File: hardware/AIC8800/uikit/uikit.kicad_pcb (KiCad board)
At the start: 2 copper layers, 36 parts, among them J1 Conn_01x20, J2 Conn_01x20, J3 Conn_01x10, J4 Conn_01x06, J5 USB_C_Receptacle_USB2.0, J6 Micro_SD_Card, J7 PJ-393-USA, U1 AIC1000A, U2 CH340N

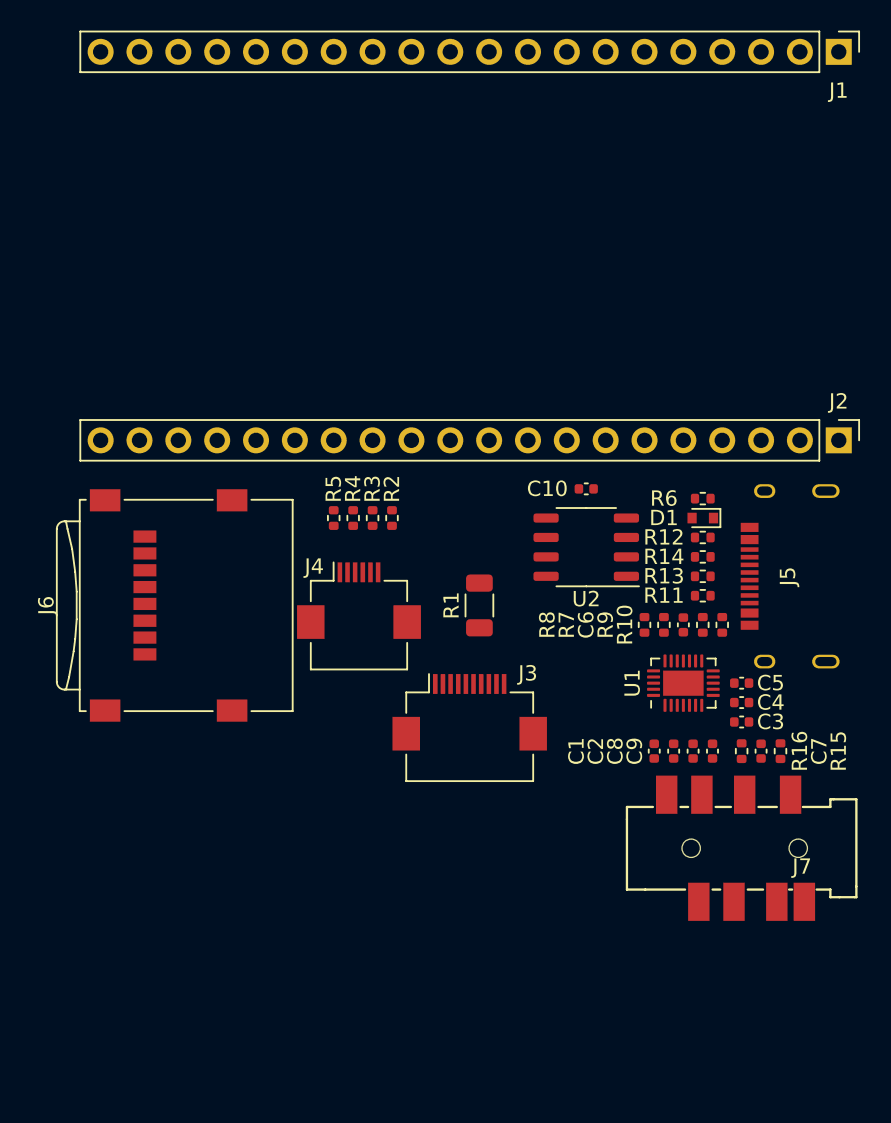
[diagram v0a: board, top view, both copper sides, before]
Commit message: [hardware/AIC8800/uikit] update PCB
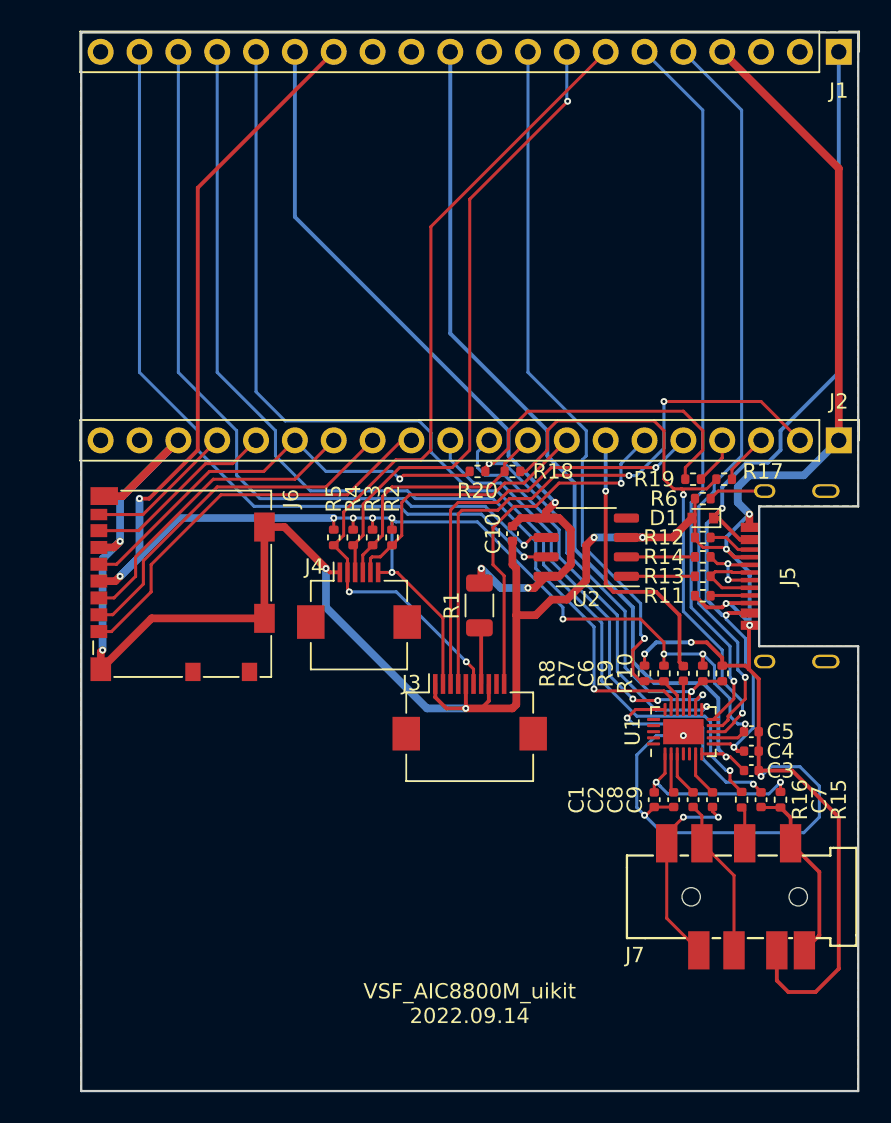
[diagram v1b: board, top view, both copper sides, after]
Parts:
- added R17: 0, Resistor_SMD:R_0402_1005Metric, F.Cu at (245.2, 118.1)
- added R18: NC, Resistor_SMD:R_0402_1005Metric, F.Cu at (231.4, 117.6)
- added R19: 0, Resistor_SMD:R_0402_1005Metric, F.Cu at (243.2, 118.1)
- added R20: NC, Resistor_SMD:R_0402_1005Metric, F.Cu at (229.1, 117.6)
- J6: value Micro_SD_Card -> Micro_SD_Card_Det; footprint Connector_Card:microSD_HC_Wuerth_693072010801 -> Connector_Card:microSD_HC_Molex_104031-0811
- moved C10 5.64 mm to (231.4, 121.7), turned to -90 degrees
- moved C5 3.24 mm to (247.0, 134.6)
- moved C3 3.24 mm to (247.0, 137.2), turned to 180 degrees
- moved C4 3.24 mm to (247.0, 135.9)
- moved C1 3.18 mm to (240.7, 139.1)
- moved C2 3.18 mm to (241.9, 139.1)
- moved C7 3.18 mm to (247.7, 139.1)
- moved C8 3.18 mm to (243.2, 139.1)
- moved C9 3.18 mm to (244.5, 139.1)
- moved R15 3.18 mm to (248.9, 139.1)
- moved R16 3.18 mm to (246.4, 139.1)
- moved U1 3.18 mm to (242.6, 134.6)
- moved C6 3.17 mm to (242.6, 130.8)
- moved R10 3.17 mm to (245.1, 130.8)
- moved R7 3.17 mm to (241.3, 130.8)
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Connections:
- R10 pad 2: /A2 -> /I2S_DIN
- R9 pad 2: /A2 -> /I2S_DIN
- U1 pad 10: /A1 -> /I2S_BCK
- U1 pad 15: /A2 -> /I2S_DIN
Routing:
- net GND: track 0.00 -> 234.5 mm, vias 0 -> 15
- net /VCC: track 0.00 -> 112.9 mm, vias 0 -> 11
- net /B4: track 0.00 -> 70.5 mm, vias 0 -> 1
- net /AU_PWR: track 0.00 -> 64.6 mm, vias 0 -> 1
- net /USB_5V: track 0.00 -> 59.4 mm, vias 0 -> 3
- net /V13: track 0.00 -> 58.7 mm, vias 0 -> 1
- net /B1: track 0.00 -> 55.3 mm, vias 0 -> 2
- net /B7: track 0.00 -> 53.3 mm, vias 0 -> 1
- net /V33: track 0.00 -> 52.4 mm, vias 0 -> 3
- net /B6: track 0.00 -> 51.6 mm, vias 0 -> 1
- net /AU_SDA: track 0.00 -> 49.3 mm, vias 0 -> 1
- net /AU_SLEEP: track 0.00 -> 48.8 mm, vias 0 -> 1
- net /AU_SCL: track 0.00 -> 47.3 mm, vias 0 -> 1
- net /I2S_DIN: track 0.00 -> 47.0 mm, vias 0 -> 2
- net /B2: track 0.00 -> 41.9 mm, vias 0 -> 1
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- added copper zone on B.Cu, net GND
- added copper zone on F.Cu, net GND
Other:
- board outline added: 50.8 x 69.2 mm
- board text added: "VSF_AIC8800M_uikit 2022.09.14"

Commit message: [hardware/AIC8800/uikit] update PCB
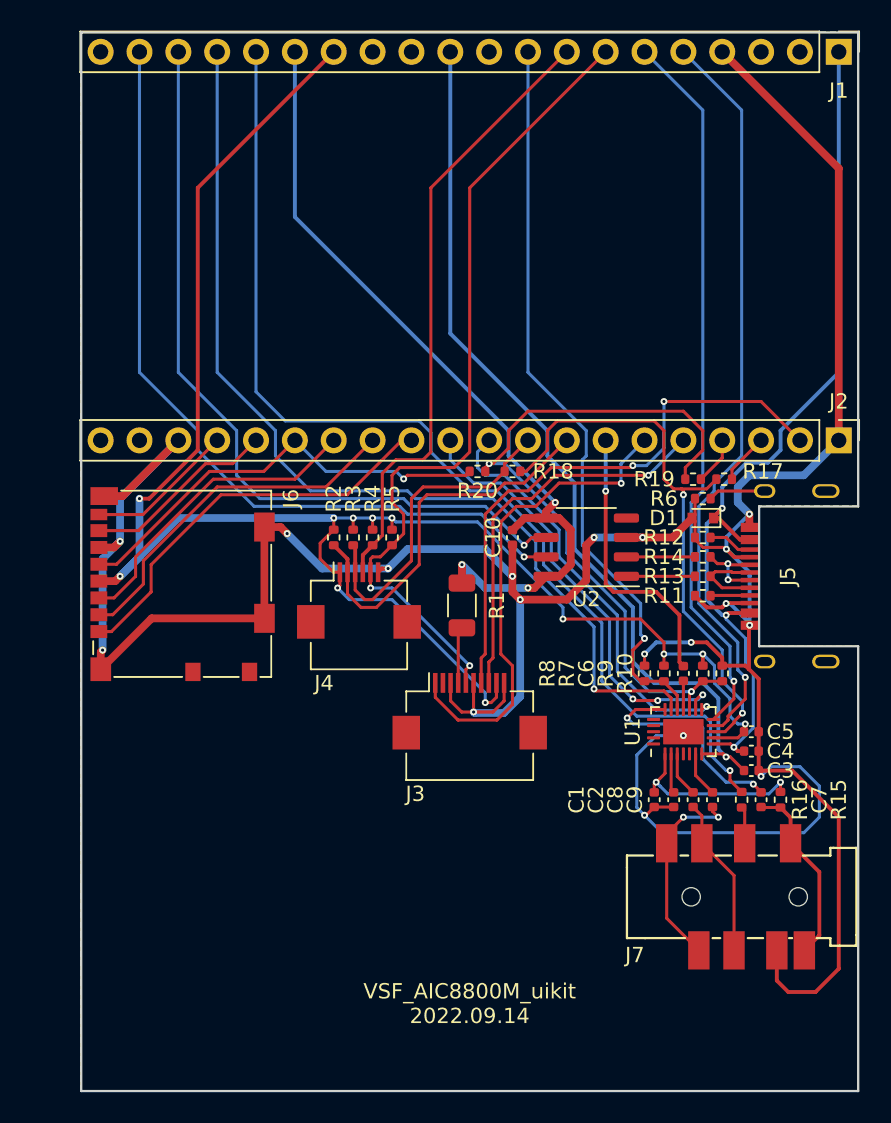
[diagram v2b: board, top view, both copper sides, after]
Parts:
- J3: footprint Connector_FFC-FPC:Hirose_FH12-10S-0.5SH_1x10-1MP_P0.50mm_Horizontal -> VSF:Hirose_FH12-10S-0.5SH_1x10-1MP_P0.50mm_Horizontal_Reverse
- J4: footprint Connector_FFC-FPC:Hirose_FH12-6S-0.5SH_1x06-1MP_P0.50mm_Horizontal -> VSF:Hirose_FH12-6S-0.5SH_1x06-1MP_P0.50mm_Horizontal_Reverse
- moved R2 3.81 mm to (219.7, 121.9)
- moved R5 3.81 mm to (223.5, 121.9)
- moved R3 1.27 mm to (221.0, 121.9)
- moved R4 1.27 mm to (222.2, 121.9)
- moved R1 1.14 mm to (228.1, 126.4)
- moved C10 0.25 mm to (231.4, 121.9)
- moved J4 0.06 mm to (221.4, 126.1)
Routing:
- net /A4: track 23.6 -> 31.7 mm
- net /A6: track 18.2 -> 25.2 mm
- net /VCC: track 112.9 -> 119.5 mm, vias 11 -> 12
- net /A7: track 16.8 -> 21.5 mm
- net /A3: track 28.5 -> 25.4 mm
- net /A0: track 39.4 -> 37.6 mm
- net /V33: track 52.4 -> 54.1 mm
- net GND: track 234.5 -> 232.8 mm, vias 15 -> 18
- net /B2: track 41.9 -> 40.6 mm, vias 1 -> 0
- net /B1: track 55.3 -> 54.3 mm

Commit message: [hardware/AIC8800/uikit] minor tweak
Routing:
- net /B2: track 40.6 -> 41.1 mm
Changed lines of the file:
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@@
   (segment (start 243.84 129.54) (end 243.84 130.3) (width 0.254) (layer "F.Cu") (net 8))
   (segment (start 230.35 131.43) (end 230.35 132.362) (width 0.2) (layer "F.Cu") (net 8))
-  (segment (start 218.821 123.317) (end 218.821 122.299) (width 0.2) (layer "F.Cu") (net 8))
+  (segment (start 218.948 122.172) (end 219.71 121.41) (width 0.2) (layer "F.Cu") (net 8))
   (segment (start 220.111 124.191) (end 220.111 125.075) (width 0.2) (layer "F.Cu") (net 8))
   (segment (start 205.427 124.773) (end 205.74 124.46) (width 0.508) (layer "F.Cu") (net 8))
-  (segment (start 218.821 122.299) (end 219.71 121.41) (width 0.2) (layer "F.Cu") (net 8))
   (segment (start 229.997 132.715) (end 229.616 132.715) (width 0.2) (layer "F.Cu") (net 8))
   (segment (start 223.52 121.41) (end 223.52 120.65) (width 0.2) (layer "F.Cu") (net 8))
   (segment (start 244.52 135.02) (end 246.135 135.02) (width 0.2) (layer "F.Cu") (net 8))
+  (segment (start 218.948 122.936) (end 218.948 122.172) (width 0.2) (layer "F.Cu") (net 8))
   (segment (start 241.3 128.778) (end 241.3 129.54) (width 0.2) (layer "F.Cu") (net 8))
   (segment (start 246.535 134.62) (end 246.535 134.194479) (width 0.2) (layer "F.Cu") (net 8))
@@
   (segment (start 230.35 132.362) (end 229.997 132.715) (width 0.2) (layer "F.Cu") (net 8))
   (segment (start 220.111 125.075) (end 219.964 125.222) (width 0.2) (layer "F.Cu") (net 8))
-  (segment (start 220.111 124.191) (end 219.695 124.191) (width 0.2) (layer "F.Cu") (net 8))
   (segment (start 241.3 130.3) (end 241.3 129.54) (width 0.2) (layer "F.Cu") (net 8))
+  (segment (start 220.111 124.191) (end 220.111 124.099) (width 0.2) (layer "F.Cu") (net 8))
   (segment (start 239.776 127.254) (end 241.3 128.778) (width 0.2) (layer "F.Cu") (net 8))
   (segment (start 210.82 116.205) (end 207.645 119.38) (width 0.254) (layer "F.Cu") (net 8))
   (segment (start 246.135 135.02) (end 246.535 134.62) (width 0.2) (layer "F.Cu") (net 8))
-  (segment (start 219.695 124.191) (end 218.821 123.317) (width 0.2) (layer "F.Cu") (net 8))
+  (segment (start 220.111 124.099) (end 218.948 122.936) (width 0.2) (layer "F.Cu") (net 8))
   (via (at 219.964 125.222) (size 0.45212) (drill 0.2032) (layers "F.Cu" "B.Cu") (net 8))
   (via (at 241.3 129.54) (size 0.45212) (drill 0.2032) (layers "F.Cu" "B.Cu") (net 8))
@@
   (segment (start 222.111 123.329) (end 222.25 123.19) (width 0.2) (layer "F.Cu") (net 22))
   (segment (start 228.35 131.43) (end 228.35 130.552) (width 0.2) (layer "F.Cu") (net 22))
-  (segment (start 224.028 117.348) (end 223.52 117.856) (width 0.2) (layer "F.Cu") (net 22))
-  (segment (start 224.282 121.668) (end 223.52 122.43) (width 0.2) (layer "F.Cu") (net 22))
+  (segment (start 223.52 122.43) (end 222.885 121.795) (width 0.2) (layer "F.Cu") (net 22))
   (segment (start 222.123 125.222) (end 222.111 125.21) (width 0.2) (layer "F.Cu") (net 22))
   (segment (start 228.6 116.332) (end 227.584 117.348) (width 0.2) (layer "F.Cu") (net 22))
   (segment (start 227.584 117.348) (end 224.028 117.348) (width 0.2) (layer "F.Cu") (net 22))
-  (segment (start 223.52 119.634) (end 224.282 120.396) (width 0.2) (layer "F.Cu") (net 22))
   (segment (start 228.35 130.552) (end 228.6 130.302) (width 0.2) (layer "F.Cu") (net 22))
   (segment (start 223.518 122.43) (end 223.52 122.43) (width 0.2) (layer "F.Cu") (net 22))
   (segment (start 222.111 124.191) (end 222.111 123.329) (width 0.2) (layer "F.Cu") (net 22))
+  (segment (start 222.885 118.491) (end 224.028 117.348) (width 0.2) (layer "F.Cu") (net 22))
   (segment (start 222.25 123.19) (end 222.758 123.19) (width 0.2) (layer "F.Cu") (net 22))
+  (segment (start 222.885 121.795) (end 222.885 118.491) (width 0.2) (layer "F.Cu") (net 22))
   (segment (start 222.758 123.19) (end 223.518 122.43) (width 0.2) (layer "F.Cu") (net 22))
-  (segment (start 223.52 117.856) (end 223.52 119.634) (width 0.2) (layer "F.Cu") (net 22))
   (segment (start 228.6 99.06) (end 228.6 116.332) (width 0.2) (layer "F.Cu") (net 22))
   (segment (start 222.111 125.21) (end 222.111 124.191) (width 0.2) (layer "F.Cu") (net 22))
-  (segment (start 224.282 120.396) (end 224.282 121.668) (width 0.2) (layer "F.Cu") (net 22))
   (segment (start 237.49 90.17) (end 228.6 99.06) (width 0.2) (layer "F.Cu") (net 22))
   (via (at 222.123 125.222) (size 0.45212) (drill 0.2032) (layers "F.Cu" "B.Cu") (net 22))
@@
   (segment (start 223.52 125.222) (end 222.123 125.222) (width 0.2) (layer "B.Cu") (net 22))
   (segment (start 228.6 130.302) (end 223.52 125.222) (width 0.2) (layer "B.Cu") (net 22))
-  (segment (start 223.774 116.84) (end 222.885 117.729) (width 0.2) (layer "F.Cu") (net 23))
-  (segment (start 222.885 117.729) (end 222.885 121.795) (width 0.2) (layer "F.Cu") (net 23))
+  (segment (start 222.25 122.43) (end 221.615 121.795) (width 0.2) (layer "F.Cu") (net 23))
   (segment (start 226.06 99.06) (end 226.06 116.332) (width 0.2) (layer "F.Cu") (net 23))
   (segment (start 221.611 124.191) (end 221.611 123.069) (width 0.254) (layer "F.Cu") (net 23))
+  (segment (start 221.615 118.999) (end 223.774 116.84) (width 0.2) (layer "F.Cu") (net 23))
+  (segment (start 221.615 121.795) (end 221.615 118.999) (width 0.2) (layer "F.Cu") (net 23))
   (segment (start 234.95 90.17) (end 226.06 99.06) (width 0.2) (layer "F.Cu") (net 23))
   (segment (start 226.06 116.332) (end 225.552 116.84) (width 0.2) (layer "F.Cu") (net 23))
   (segment (start 221.611 123.069) (end 222.25 122.43) (width 0.254) (layer "F.Cu") (net 23))
-  (segment (start 222.885 121.795) (end 222.25 122.43) (width 0.2) (layer "F.Cu") (net 23))
   (segment (start 225.552 116.84) (end 223.774 116.84) (width 0.2) (layer "F.Cu") (net 23))
   (segment (start 241.3 131.369975) (end 242.17 132.239975) (width 0.2) (layer "F.Cu") (net 24))
@@
   (segment (start 238.506 118.38156) (end 238.48794 118.3635) (width 0.2) (layer "B.Cu") (net 37))
   (segment (start 230.124 119.126) (end 225.806 119.126) (width 0.2) (layer "F.Cu") (net 38))
-  (segment (start 221.488 126.492) (end 220.611 125.615) (width 0.2) (layer "F.Cu") (net 38))
+  (segment (start 225.806 119.126) (end 224.79 120.142) (width 0.2) (layer "F.Cu") (net 38))
   (segment (start 220.611 124.191) (end 220.611 123.331) (width 0.254) (layer "F.Cu") (net 38))
   (segment (start 230.886 118.364) (end 230.124 119.126) (width 0.2) (layer "F.Cu") (net 38))
+  (segment (start 234.95 115.57) (end 232.156 118.364) (width 0.2) (layer "F.Cu") (net 38))
   (segment (start 220.611 123.331) (end 219.71 122.43) (width 0.254) (layer "F.Cu") (net 38))
-  (segment (start 225.806 119.126) (end 225.298 119.634) (width 0.2) (layer "F.Cu") (net 38))
-  (segment (start 225.298 119.634) (end 225.298 123.698) (width 0.2) (layer "F.Cu") (net 38))
-  (segment (start 225.298 123.698) (end 222.504 126.492) (width 0.2) (layer "F.Cu") (net 38))
-  (segment (start 234.95 115.57) (end 232.156 118.364) (width 0.2) (layer "F.Cu") (net 38))
+  (segment (start 224.79 120.142) (end 224.79 124.206) (width 0.2) (layer "F.Cu") (net 38))
+  (segment (start 222.504 126.492) (end 221.488 126.492) (width 0.2) (layer "F.Cu") (net 38))
+  (segment (start 224.79 124.206) (end 222.504 126.492) (width 0.2) (layer "F.Cu") (net 38))
   (segment (start 220.611 125.615) (end 220.611 124.191) (width 0.2) (layer "F.Cu") (net 38))
-  (segment (start 222.504 126.492) (end 221.488 126.492) (width 0.2) (layer "F.Cu") (net 38))
+  (segment (start 221.488 126.492) (end 220.611 125.615) (width 0.2) (layer "F.Cu") (net 38))
   (segment (start 232.156 118.364) (end 230.886 118.364) (width 0.2) (layer "F.Cu") (net 38))
-  (segment (start 229.868 118.618) (end 225.552 118.618) (width 0.2) (layer "F.Cu") (net 39))
-  (segment (start 224.79 123.444) (end 222.25 125.984) (width 0.2) (layer "F.Cu") (net 39))
-  (segment (start 224.79 119.38) (end 224.79 123.444) (width 0.2) (layer "F.Cu") (net 39))
   (segment (start 221.111 125.353) (end 221.111 124.191) (width 0.2) (layer "F.Cu") (net 39))
+  (segment (start 221.742 125.984) (end 221.111 125.353) (width 0.2) (layer "F.Cu") (net 39))
+  (segment (start 224.282 120.084315) (end 224.282 123.952) (width 0.2) (layer "F.Cu") (net 39))
+  (segment (start 221.111 122.561) (end 220.98 122.43) (width 0.254) (layer "F.Cu") (net 39))
+  (segment (start 230.884 117.602) (end 229.868 118.618) (width 0.2) (layer "F.Cu") (net 39))
+  (segment (start 224.282 123.952) (end 222.25 125.984) (width 0.2) (layer "F.Cu") (net 39))
+  (segment (start 221.111 124.191) (end 221.111 122.561) (width 0.254) (layer "F.Cu") (net 39))
+  (segment (start 225.748315 118.618) (end 224.282 120.084315) (width 0.2) (layer "F.Cu") (net 39))
+  (segment (start 230.884 117.096) (end 230.884 117.602) (width 0.2) (layer "F.Cu") (net 39))
+  (segment (start 229.868 118.618) (end 225.748315 118.618) (width 0.2) (layer "F.Cu") (net 39))
   (segment (start 222.25 125.984) (end 221.742 125.984) (width 0.2) (layer "F.Cu") (net 39))
-  (segment (start 221.111 122.561) (end 220.98 122.43) (width 0.254) (layer "F.Cu") (net 39))
-  (segment (start 225.552 118.618) (end 224.79 119.38) (width 0.2) (layer "F.Cu") (net 39))
-  (segment (start 230.884 117.602) (end 229.868 118.618) (width 0.2) (layer "F.Cu") (net 39))
-  (segment (start 221.111 124.191) (end 221.111 122.561) (width 0.254) (layer "F.Cu") (net 39))
-  (segment (start 230.884 117.096) (end 230.884 117.602) (width 0.2) (layer "F.Cu") (net 39))
-  (segment (start 221.742 125.984) (end 221.111 125.353) (width 0.2) (layer "F.Cu") (net 39))
   (segment (start 232.41 115.57) (end 230.884 117.096) (width 0.2) (layer "F.Cu") (net 39))
   (segment (start 244.094 132.969) (end 243.971 132.969) (width 0.2) (layer "F.Cu") (net 40))
